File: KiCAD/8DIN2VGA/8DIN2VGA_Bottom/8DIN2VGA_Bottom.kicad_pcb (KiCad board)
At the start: 2 copper layers, 6.6 x 19.9 mm, 2 parts

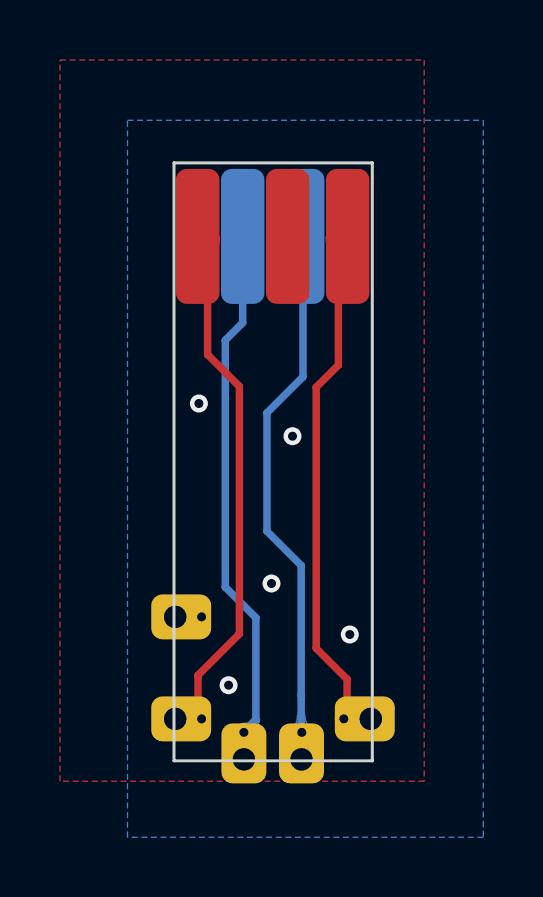
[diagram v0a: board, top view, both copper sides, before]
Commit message: Update with new 5V design
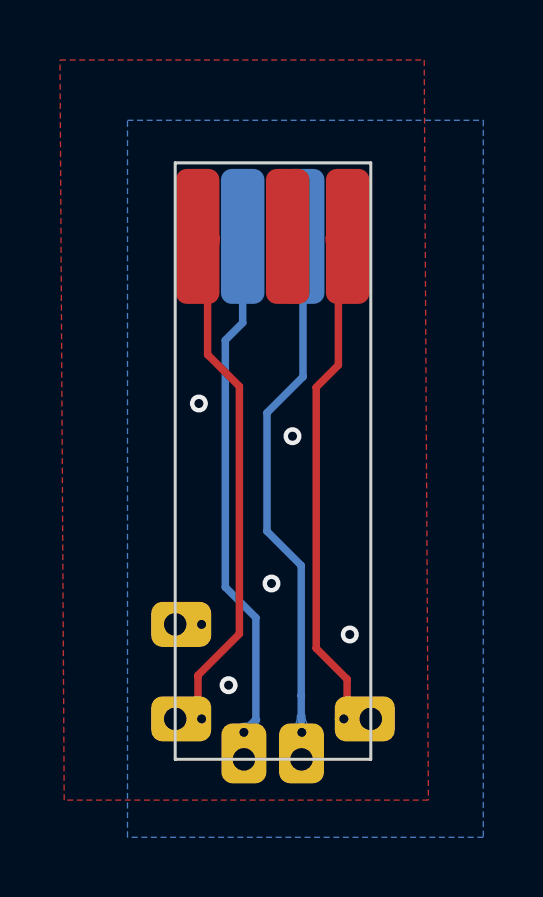
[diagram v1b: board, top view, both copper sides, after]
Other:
- board size 6.6 x 19.9 mm -> 6.5 x 19.9 mm
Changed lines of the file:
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@@
-(kicad_pcb (version 20171130) (host pcbnew "(5.1.8-0-10_14)")
+(kicad_pcb (version 20171130) (host pcbnew "(5.1.10-1-10_14)")
   (general
     (thickness 0.8)
@@
     (pad 3 thru_hole roundrect (at 3.27 -1.35 90) (size 1.5 2) (drill 0.75 (offset 0 -0.2)) (layers *.Cu *.Mask) (roundrect_rratio 0.25)
       (net 3 /Sync))
-    (pad 4 thru_hole roundrect (at -3.25 -4.75 270) (size 1.5 2) (drill 0.75 (offset 0 -0.2)) (layers *.Cu *.Mask) (roundrect_rratio 0.25)
+    (pad 4 thru_hole roundrect (at -3.25 -4.5 270) (size 1.5 2) (drill 0.75 (offset 0 -0.2)) (layers *.Cu *.Mask) (roundrect_rratio 0.25)
       (net 4 /GND))
-    (pad 4 thru_hole circle (at -2.37 -4.75 270) (size 0.6 0.6) (drill 0.3) (layers *.Cu *.Mask)
+    (pad 4 thru_hole circle (at -2.37 -4.5 270) (size 0.6 0.6) (drill 0.3) (layers *.Cu *.Mask)
       (net 4 /GND))
   )
@@
   )
   (gr_poly (pts (xy 149.25 110.27) (xy 147.76 110.27) (xy 147.76 104.34) (xy 149.25 104.34)) (layer Cmts.User) (width 0.1))
-  (gr_line (start 148.32 95.39) (end 148.32 115.32) (layer Edge.Cuts) (width 0.1))
-  (gr_line (start 141.71 95.39) (end 148.32 95.39) (layer Edge.Cuts) (width 0.1))
-  (gr_line (start 141.71 115.32) (end 141.71 95.39) (layer Edge.Cuts) (width 0.1))
-  (gr_line (start 141.71 115.32) (end 148.32 115.32) (layer Edge.Cuts) (width 0.1))
+  (gr_line (start 148.27 95.39) (end 148.27 115.27) (layer Edge.Cuts) (width 0.1))
+  (gr_line (start 141.75 95.39) (end 148.27 95.39) (layer Edge.Cuts) (width 0.1))
+  (gr_line (start 141.75 115.27) (end 141.75 95.39) (layer Edge.Cuts) (width 0.1))
+  (gr_line (start 141.75 115.27) (end 148.27 115.27) (layer Edge.Cuts) (width 0.1))
   (segment (start 144.03 114.35) (end 144.02 114.35) (width 0.25) (layer Back) (net 1))
   (segment (start 144.44 113.94) (end 144.03 114.35) (width 0.25) (layer Back) (net 1))
@@
     (polygon
       (pts
-        (xy 150.05 116) (xy 137.91 116) (xy 137.91 91.96) (xy 150.05 91.96)
+        (xy 150.19 116.63) (xy 138.05 116.63) (xy 137.91 91.96) (xy 150.05 91.96)
       )
     )
